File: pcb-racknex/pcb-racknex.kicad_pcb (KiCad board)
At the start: 2 copper layers, 33 x 56 mm, 18 parts, among them J1 Conn_I2C, J2 Conn_LED, J3 Conn_Fan, J4 Conn_ON_OFF, P1 Conn_Pi, Q1 S8050 NPN, T1 3, T2 4, U1 DS3231M

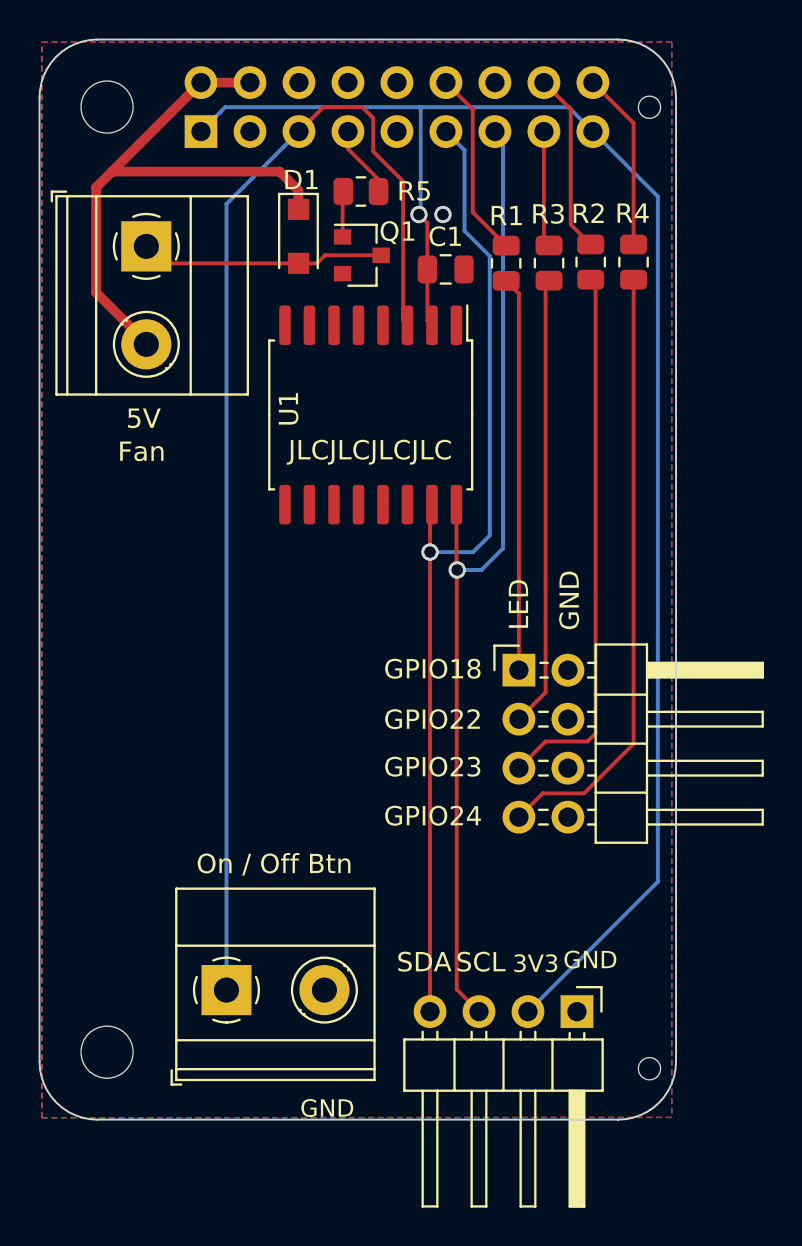
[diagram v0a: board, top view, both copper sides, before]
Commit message: Rev 2.5: optimzed footprints and layouts
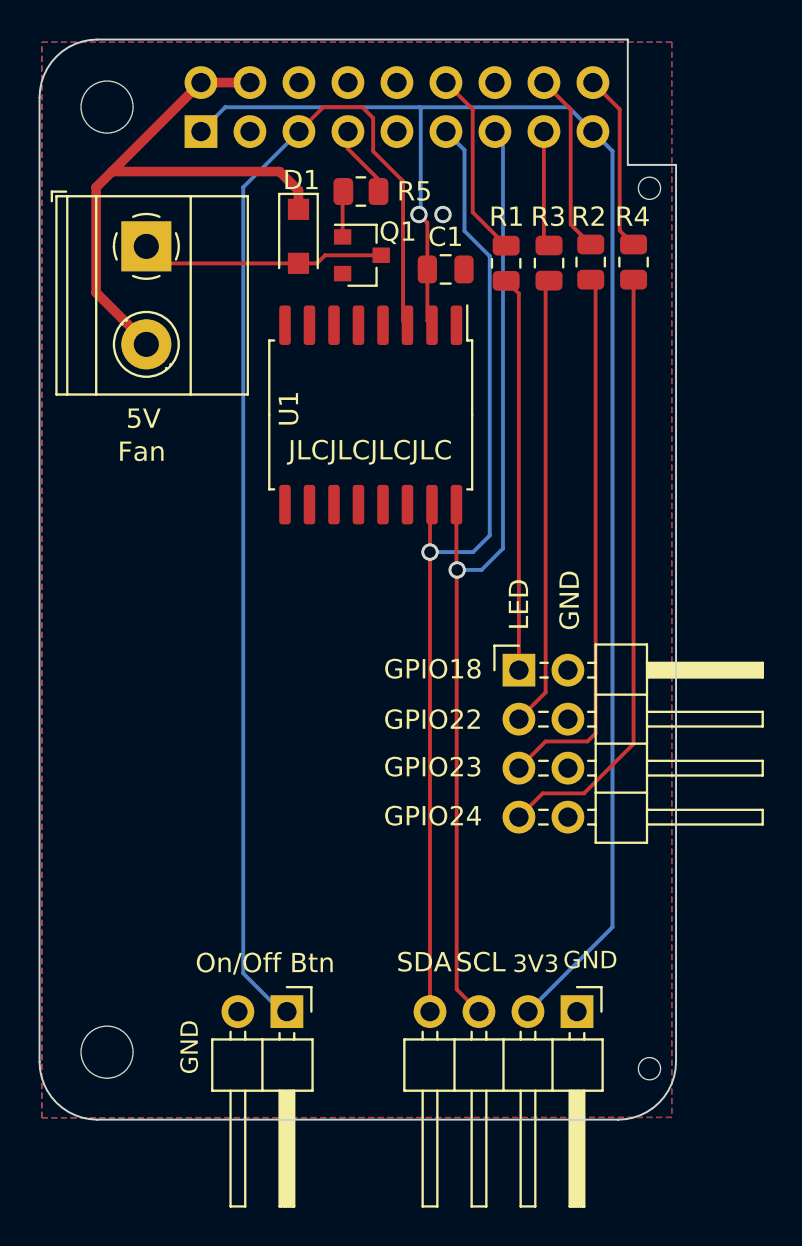
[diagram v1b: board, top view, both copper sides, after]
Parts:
- J4: footprint TerminalBlock_Phoenix:TerminalBlock_Phoenix_MKDS-1,5-2-5.08_1x02_P5.08mm_Horizontal -> Connector_PinHeader_2.54mm:PinHeader_1x02_P2.54mm_Horizontal
- moved T1 4.20 mm to (231.6, 101.7)
- moved J4 3.33 mm to (212.8, 144.4), turned to 270 degrees
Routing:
- net /GPIO3(ON_OFF): track 62.2 -> 64.1 mm
- net +3V3: track 82.9 -> 80.9 mm
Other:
- outline, holes or cut-outs redrawn
- board text added: "On/Off Btn"
- board text added: "https://github.com/bablokb/pcb-racknex Rev 2.5"
- board text removed: "On / Off Btn"
- board text removed: "https://github.com/bablokb/pcb-racknex Rev 2.3"
